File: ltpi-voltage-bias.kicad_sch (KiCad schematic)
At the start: 18 parts

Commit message: [#83609] Reannotate board
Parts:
- renumbered C67 to C151, C68 to C152, C70 to C153, C71 to C154, C73 to C155, C75 to C156, C74 to C157, C76 to C158, C69 to C159, C72 to C160, R134 to R264, R135 to R265, R138 to R266, R139 to R267, R136 to R268, R137 to R269, R140 to R270, R141 to R271
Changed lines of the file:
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@@
 		(dnp no)
 		(fields_autoplaced yes)
-		(property "Reference" "C68"
+		(property "Reference" "C152"
 			(at 191.7763 132.08 0)
 			(effects
@@
 			(project "bmc-reference-carrier-board"
 				(path "/5f636c45-3c15-4731-8931-4625e0dab7e4/5ae3d11e-bdb2-474c-9920-031cf5845646"
-					(reference "C68")
+					(reference "C152")
 					(unit 1)
 				)
@@
 		(dnp no)
 		(fields_autoplaced yes)
-		(property "Reference" "C70"
+		(property "Reference" "C153"
 			(at 191.7763 143.51 0)
 			(effects
@@
 			(project "bmc-reference-carrier-board"
 				(path "/5f636c45-3c15-4731-8931-4625e0dab7e4/5ae3d11e-bdb2-474c-9920-031cf5845646"
-					(reference "C70")
+					(reference "C153")
 					(unit 1)
 				)
@@
 		(dnp no)
 		(fields_autoplaced yes)
-		(property "Reference" "C75"
+		(property "Reference" "C156"
 			(at 191.7763 181.61 0)
 			(effects
@@
 			(project "bmc-reference-carrier-board"
 				(path "/5f636c45-3c15-4731-8931-4625e0dab7e4/5ae3d11e-bdb2-474c-9920-031cf5845646"
-					(reference "C75")
+					(reference "C156")
 					(unit 1)
 				)
@@
 		(dnp no)
 		(fields_autoplaced yes)
-		(property "Reference" "#PWR0132"
+		(property "Reference" "#PWR0304"
 			(at 248.92 127 0)
 			(effects
@@
 			(project ""
 				(path "/5f636c45-3c15-4731-8931-4625e0dab7e4/5ae3d11e-bdb2-474c-9920-031cf5845646"
-					(reference "#PWR0132")
+					(reference "#PWR0304")
 					(unit 1)
 				)
@@
 		(dnp no)
 		(fields_autoplaced yes)
-		(property "Reference" "C76"
+		(property "Reference" "C158"
 			(at 199.3963 186.69 0)
 			(effects
@@
 			(project "bmc-reference-carrier-board"
 				(path "/5f636c45-3c15-4731-8931-4625e0dab7e4/5ae3d11e-bdb2-474c-9920-031cf5845646"
-					(reference "C76")
+					(reference "C158")
 					(unit 1)
 				)
@@
 		(on_board yes)
 		(dnp no)
-		(property "Reference" "R134"
+		(property "Reference" "R264"
 			(at 203.2 125.73 90)
 			(effects
@@
 			(project ""
 				(path "/5f636c45-3c15-4731-8931-4625e0dab7e4/5ae3d11e-bdb2-474c-9920-031cf5845646"
-					(reference "R134")
+					(reference "R264")
 					(unit 1)
 				)
@@
 		(dnp no)
 		(fields_autoplaced yes)
-		(property "Reference" "C71"
+		(property "Reference" "C154"
 			(at 191.7763 158.75 0)
 			(effects
@@
 			(project "bmc-reference-carrier-board"
 				(path "/5f636c45-3c15-4731-8931-4625e0dab7e4/5ae3d11e-bdb2-474c-9920-031cf5845646"
-					(reference "C71")
+					(reference "C154")
 					(unit 1)
 				)
@@
 		(dnp no)
 		(fields_autoplaced yes)
-		(property "Reference" "C73"
+		(property "Reference" "C155"
 			(at 191.7763 171.45 0)
 			(effects
@@
 			(project "bmc-reference-carrier-board"
 				(path "/5f636c45-3c15-4731-8931-4625e0dab7e4/5ae3d11e-bdb2-474c-9920-031cf5845646"
-					(reference "C73")
+					(reference "C155")
 					(unit 1)
 				)
@@
 		(on_board yes)
 		(dnp no)
-		(property "Reference" "R138"
+		(property "Reference" "R266"
 			(at 203.2 152.4 90)
 			(effects
@@
 			(project "bmc-reference-carrier-board"
 				(path "/5f636c45-3c15-4731-8931-4625e0dab7e4/5ae3d11e-bdb2-474c-9920-031cf5845646"
-					(reference "R138")
+					(reference "R266")
 					(unit 1)
 				)
@@
 		(dnp no)
 		(fields_autoplaced yes)
-		(property "Reference" "C67"
+		(property "Reference" "C151"
 			(at 191.7763 116.84 0)
 			(effects
@@
 			(project ""
 				(path "/5f636c45-3c15-4731-8931-4625e0dab7e4/5ae3d11e-bdb2-474c-9920-031cf5845646"
-					(reference "C67")
+					(reference "C151")
 					(unit 1)
 				)
@@
 		(dnp no)
 		(fields_autoplaced yes)
-		(property "Reference" "C72"
+		(property "Reference" "C160"
 			(at 246.38 160.0136 90)
 			(effects
@@
 			(project "bmc-reference-carrier-board"
 				(path "/5f636c45-3c15-4731-8931-4625e0dab7e4/5ae3d11e-bdb2-474c-9920-031cf5845646"
-					(reference "C72")
+					(reference "C160")
 					(unit 1)
 				)
@@
 		(on_board yes)
 		(dnp no)
-		(property "Reference" "R135"
+		(property "Reference" "R265"
 			(at 203.2 133.35 90)
 			(effects
@@
 			(project "bmc-reference-carrier-board"
 				(path "/5f636c45-3c15-4731-8931-4625e0dab7e4/5ae3d11e-bdb2-474c-9920-031cf5845646"
-					(reference "R135")
+					(reference "R265")
 					(unit 1)
 				)
@@
 		(dnp no)
 		(fields_autoplaced yes)
-		(property "Reference" "#PWR0131"
+		(property "Reference" "#PWR0307"
 			(at 247.65 167.64 0)
 			(effects
@@
 			(project "bmc-reference-carrier-board"
 				(path "/5f636c45-3c15-4731-8931-4625e0dab7e4/5ae3d11e-bdb2-474c-9920-031cf5845646"
-					(reference "#PWR0131")
+					(reference "#PWR0307")
 					(unit 1)
 				)
@@
 		(dnp no)
 		(fields_autoplaced yes)
-		(property "Reference" "#PWR0133"
+		(property "Reference" "#PWR0305"
 			(at 248.92 153.67 0)
 			(effects
@@
 			(project "bmc-reference-carrier-board"
 				(path "/5f636c45-3c15-4731-8931-4625e0dab7e4/5ae3d11e-bdb2-474c-9920-031cf5845646"
-					(reference "#PWR0133")
+					(reference "#PWR0305")
 					(unit 1)
 				)
@@
 		(dnp no)
 		(fields_autoplaced yes)
-		(property "Reference" "#PWR0128"
+		(property "Reference" "#PWR0306"
 			(at 247.65 140.97 0)
 			(effects
@@
 			(project ""
 				(path "/5f636c45-3c15-4731-8931-4625e0dab7e4/5ae3d11e-bdb2-474c-9920-031cf5845646"
-					(reference "#PWR0128")
+					(reference "#PWR0306")
 					(unit 1)
 				)
@@
 		(dnp no)
 		(fields_autoplaced yes)
-		(property "Reference" "C69"
+		(property "Reference" "C159"
 			(at 246.38 133.3436 90)
 			(effects
@@
 			(project ""
 				(path "/5f636c45-3c15-4731-8931-4625e0dab7e4/5ae3d11e-bdb2-474c-9920-031cf5845646"
-					(reference "C69")
+					(reference "C159")
 					(unit 1)
 				)
@@
 		(dnp no)
 		(fields_autoplaced yes)
-		(property "Reference" "R140"
+		(property "Reference" "R270"
 			(at 236.22 152.4 90)
 			(effects
@@
 			(project "bmc-reference-carrier-board"
 				(path "/5f636c45-3c15-4731-8931-4625e0dab7e4/5ae3d11e-bdb2-474c-9920-031cf5845646"
-					(reference "R140")
+					(reference "R270")
 					(unit 1)
 				)
@@
 		(dnp no)
 		(fields_autoplaced yes)
-		(property "Reference" "R136"
+		(property "Reference" "R268"
 			(at 236.22 125.73 90)
 			(effects
@@
 			(project ""
 				(path "/5f636c45-3c15-4731-8931-4625e0dab7e4/5ae3d11e-bdb2-474c-9920-031cf5845646"
-					(reference "R136")
+					(reference "R268")
 					(unit 1)
 				)
@@
 		(dnp no)
 		(fields_autoplaced yes)
-		(property "Reference" "R137"
+		(property "Reference" "R269"
 			(at 236.22 133.35 90)
 			(effects
@@
 			(project "bmc-reference-carrier-board"
 				(path "/5f636c45-3c15-4731-8931-4625e0dab7e4/5ae3d11e-bdb2-474c-9920-031cf5845646"
-					(reference "R137")
+					(reference "R269")
 					(unit 1)
 				)
@@
 		(on_board yes)
 		(dnp no)
-		(property "Reference" "R139"
+		(property "Reference" "R267"
 			(at 203.2 160.02 90)
 			(effects
@@
 			(project "bmc-reference-carrier-board"
 				(path "/5f636c45-3c15-4731-8931-4625e0dab7e4/5ae3d11e-bdb2-474c-9920-031cf5845646"
-					(reference "R139")
+					(reference "R267")
 					(unit 1)
 				)
@@
 		(dnp no)
 		(fields_autoplaced yes)
-		(property "Reference" "R141"
+		(property "Reference" "R271"
 			(at 236.22 160.02 90)
 			(effects
@@
 			(project "bmc-reference-carrier-board"
 				(path "/5f636c45-3c15-4731-8931-4625e0dab7e4/5ae3d11e-bdb2-474c-9920-031cf5845646"
-					(reference "R141")
+					(reference "R271")
 					(unit 1)
 				)
@@
 		(dnp no)
 		(fields_autoplaced yes)
-		(property "Reference" "C74"
+		(property "Reference" "C157"
 			(at 199.3963 176.53 0)
 			(effects
@@
 			(project "bmc-reference-carrier-board"
 				(path "/5f636c45-3c15-4731-8931-4625e0dab7e4/5ae3d11e-bdb2-474c-9920-031cf5845646"
-					(reference "C74")
+					(reference "C157")
 					(unit 1)
 				)

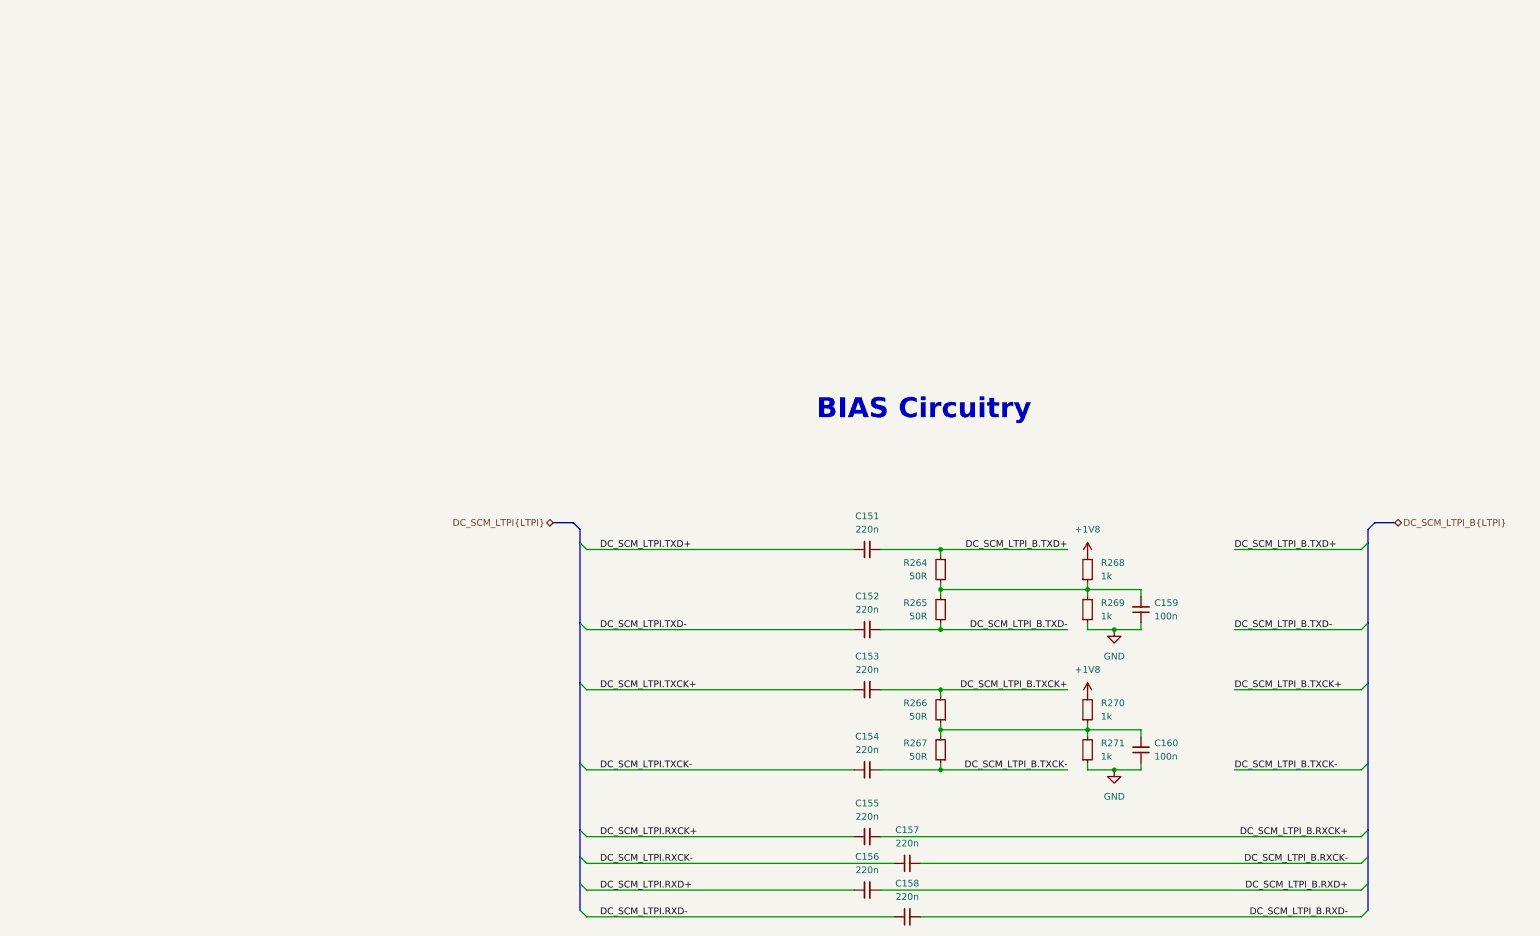
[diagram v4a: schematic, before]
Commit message: [#83736] Move LTPI bias from TX to RX, minor refactor
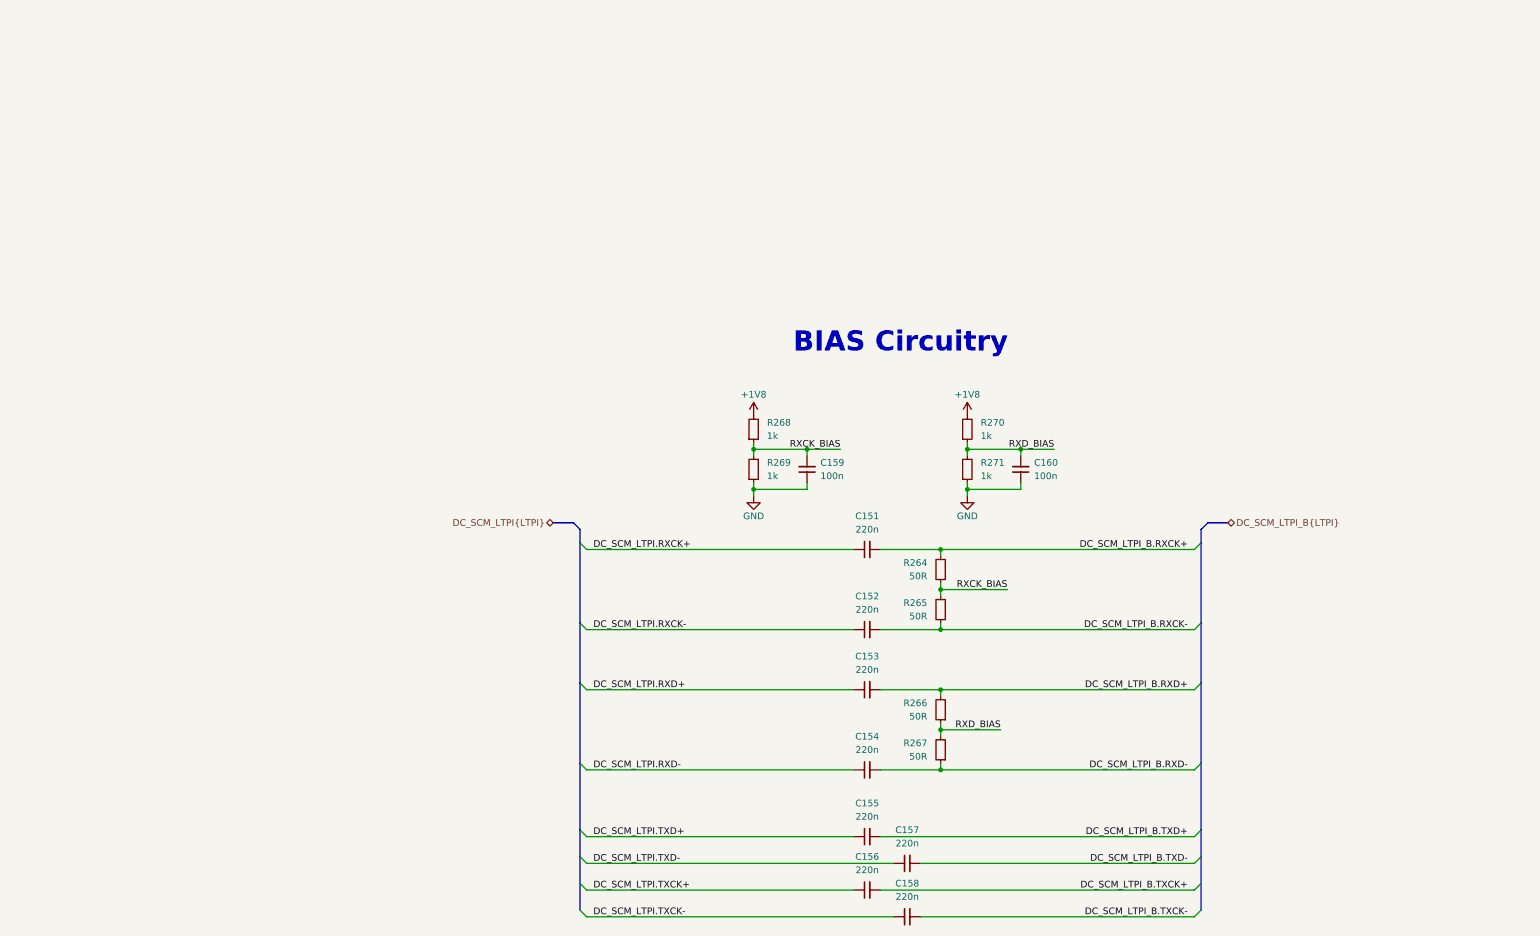
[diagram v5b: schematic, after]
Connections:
- net DC_SCM_LTPI.RXCK+: now also C151.1; no longer C155.1
- net DC_SCM_LTPI.RXCK-: now also C152.1; no longer C157.1
- net DC_SCM_LTPI.RXD+: now also C153.1; no longer C156.1
- net DC_SCM_LTPI.RXD-: now also C154.1; no longer C158.1
- net DC_SCM_LTPI.TXCK+: now also C156.1; no longer C153.1
- net DC_SCM_LTPI.TXCK-: now also C158.1; no longer C154.1
- net DC_SCM_LTPI.TXD+: now also C155.1; no longer C151.1
- net DC_SCM_LTPI.TXD-: now also C157.1; no longer C152.1
- net DC_SCM_LTPI_B.RXCK+: now also C151.2, R264.2; no longer C155.2
- net DC_SCM_LTPI_B.RXCK-: now also C152.2, R265.1; no longer C157.2
- net DC_SCM_LTPI_B.RXD+: now also C153.2, R266.2; no longer C156.2
- net DC_SCM_LTPI_B.RXD-: now also C154.2, R267.1; no longer C158.2
- net DC_SCM_LTPI_B.TXCK+: now also C156.2; no longer C153.2, R266.2
- net DC_SCM_LTPI_B.TXCK-: now also C158.2; no longer C154.2, R267.1
- net DC_SCM_LTPI_B.TXD+: now also C155.2; no longer C151.2, R264.2
- net DC_SCM_LTPI_B.TXD-: now also C157.2; no longer C152.2, R265.1
- net RXCK_BIAS: now reaches C159.2, R264.1, R265.2, R268.1, R269.2
- net RXD_BIAS: now reaches C160.2, R266.1, R267.2, R270.1, R271.2
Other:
- moved on the sheet: C159, C160, R268, R269, R270, R271
